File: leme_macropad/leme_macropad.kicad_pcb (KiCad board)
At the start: 4 copper layers, 99.9 x 63.9 mm, 90 parts, among them J1 OLED display, J2 USB_C_Receptacle_USB2.0_16P, SW1 SW_Push, SW2 SW_Push, SW3 SW_Push, SW4 RotaryEncoder_Switch, SW5 SW_Push, SW6 SW_Push, SW7 SW_Push, SW8 SW_Push, SW9 SW_Push, U0 W25Q128JVS, U1 USBLC6-2SC6, U2 NCP1117-3.3_SOT223, U3 RP2040, Y0 ABM8-272-T3

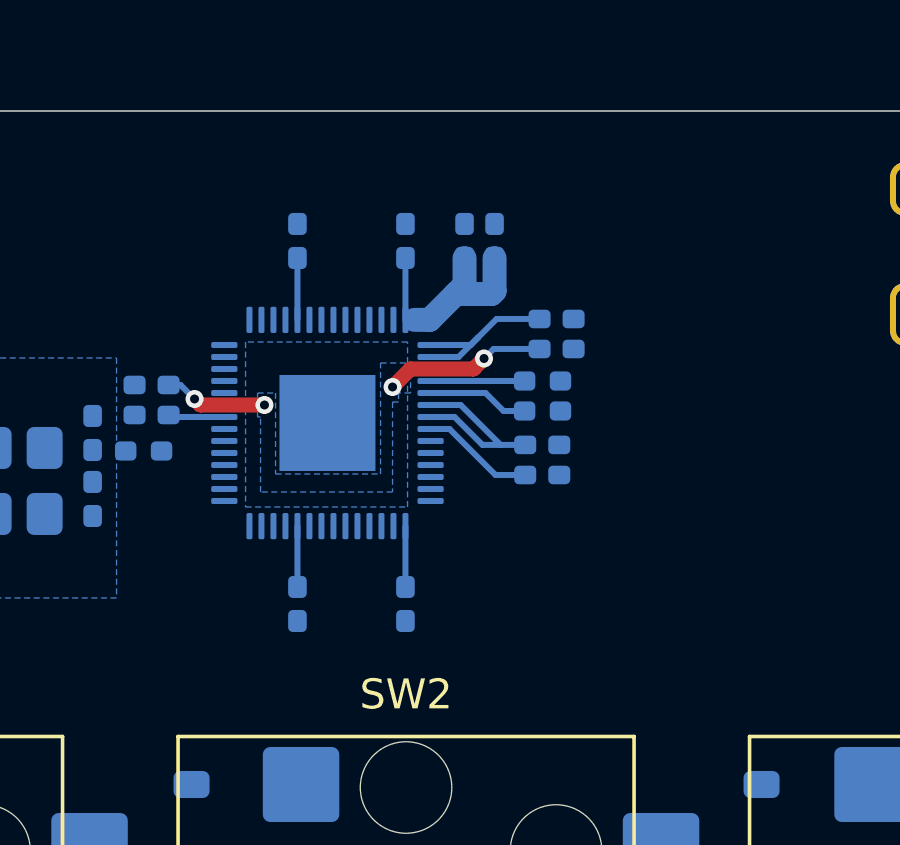
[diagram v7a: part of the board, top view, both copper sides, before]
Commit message: Routes GND for RP2040 and it's decoupling caps
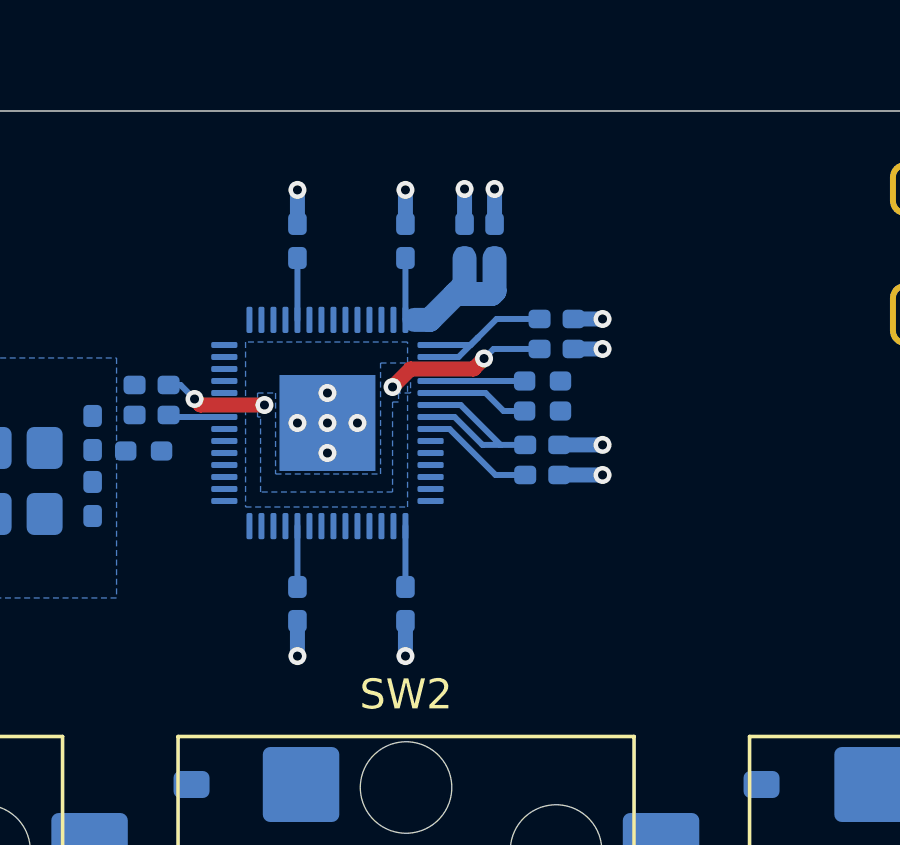
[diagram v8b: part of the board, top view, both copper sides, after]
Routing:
- net GND: track 0.03 -> 12.8 mm, vias 0 -> 15
- added copper zone on In1.Cu, net GND
- added copper zone on In2.Cu, net GND
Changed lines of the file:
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@@
 		)
+	)
+	(via
+		(at 134.43 75.4)
+		(size 0.6)
+		(drill 0.3)
+		(layers "F.Cu" "B.Cu")
+		(net 2)
+	)
+	(via
+		(at 144.6 76.129937)
+		(size 0.6)
+		(drill 0.3)
+		(layers "F.Cu" "B.Cu")
+		(net 2)
+	)
+	(via
+		(at 141 67.6)
+		(size 0.6)
+		(drill 0.3)
+		(layers "F.Cu" "B.Cu")
+		(net 2)
+	)
+	(via
+		(at 134.43 67.63)
+		(size 0.6)
+		(drill 0.3)
+		(layers "F.Cu" "B.Cu")
+		(net 2)
+	)
+	(via
+		(at 140 67.6)
+		(size 0.6)
+		(drill 0.3)
+		(layers "F.Cu" "B.Cu")
+		(net 2)
+	)
+	(via
+		(at 135.43 76.4)
+		(size 0.6)
+		(drill 0.3)
+		(layers "F.Cu" "B.Cu")
+		(net 2)
+	)
+	(via
+		(at 138.03 67.63)
+		(size 0.6)
+		(drill 0.3)
+		(layers "F.Cu" "B.Cu")
+		(net 2)
+	)
+	(via
+		(at 136.43 75.4)
+		(size 0.6)
+		(drill 0.3)
+		(layers "F.Cu" "B.Cu")
+		(net 2)
+	)
+	(via
+		(at 138.03 83.17)
+		(size 0.6)
+		(drill 0.3)
+		(layers "F.Cu" "B.Cu")
+		(net 2)
+	)
+	(via
+		(at 134.43 83.17)
+		(size 0.6)
+		(drill 0.3)
+		(layers "F.Cu" "B.Cu")
+		(net 2)
+	)
+	(via
+		(at 135.43 75.4)
+		(size 0.6)
+		(drill 0.3)
+		(layers "F.Cu" "B.Cu")
+		(net 2)
+	)
+	(via
+		(at 135.43 74.4)
+		(size 0.6)
+		(drill 0.3)
+		(layers "F.Cu" "B.Cu")
+		(net 2)
+	)
+	(via
+		(at 144.6 77.1325)
+		(size 0.6)
+		(drill 0.3)
+		(layers "F.Cu" "B.Cu")
+		(net 2)
+	)
+	(via
+		(at 144.6 72.9325)
+		(size 0.6)
+		(drill 0.3)
+		(layers "F.Cu" "B.Cu")
+		(net 2)
+	)
+	(via
+		(at 144.6 71.9325)
+		(size 0.6)
+		(drill 0.3)
+		(layers "F.Cu" "B.Cu")
+		(net 2)
+	)
+	(segment
+		(start 138.03 83.17)
+		(end 138.03 82)
+		(width 0.5)
+		(layer "B.Cu")
+		(net 2)
+	)
+	(segment
+		(start 144.6 72.9325)
+		(end 143.635 72.9325)
+		(width 0.5)
+		(layer "B.Cu")
+		(net 2)
+	)
+	(segment
+		(start 138.03 67.63)
+		(end 138.03 68.765)
+		(width 0.5)
+		(layer "B.Cu")
+		(net 2)
+	)
+	(segment
+		(start 134.43 67.63)
+		(end 134.43 68.765)
+		(width 0.5)
+		(layer "B.Cu")
+		(net 2)
+	)
+	(segment
+		(start 134.43 83.17)
+		(end 134.43 82)
+		(width 0.5)
+		(layer "B.Cu")
+		(net 2)
+	)
+	(segment
+		(start 141 68.765)
+		(end 141 67.6)
+		(width 0.5)
+		(layer "B.Cu")
+		(net 2)
+	)
+	(segment
+		(start 140 68.765)
+		(end 140 67.6)
+		(width 0.5)
+		(layer "B.Cu")
+		(net 2)
+	)
+	(segment
+		(start 135.43 75.4)
+		(end 135.43 74.43)
+		(width 0.5)
+		(layer "B.Cu")
+		(net 2)
 	)
 	(segment
 		(start 135.43 75.4)
 		(end 135.4 75.4)
-		(width 0.8)
+		(width 0.5)
+		(layer "B.Cu")
+		(net 2)
+	)
+	(segment
+		(start 144.6 71.9325)
+		(end 143.635 71.9325)
+		(width 0.5)
+		(layer "B.Cu")
+		(net 2)
+	)
+	(segment
+		(start 135.43 74.43)
+		(end 135.4 74.4)
+		(width 0.5)
+		(layer "B.Cu")
+		(net 2)
+	)
+	(segment
+		(start 144.6 76.129937)
+		(end 143.157144 76.129937)
+		(width 0.5)
+		(layer "B.Cu")
+		(net 2)
+	)
+	(segment
+		(start 144.6 77.1325)
+		(end 143.157144 77.1325)
+		(width 0.5)
 		(layer "B.Cu")
 		(net 2)
@@
 		(layer "B.Cu")
 		(hatch edge 0.5)
-		(priority 4)
+		(priority 5)
 		(connect_pads
 			(clearance 0.5)
@@
 			(thermal_gap 0.5)
 			(thermal_bridge_width 0.5)
+			(smoothing fillet)
+			(radius 0.5)
 		)
 		(polygon
@@
 			)
 		)
+	)
+	(zone
+		(net 2)
+		(net_name "GND")
+		(layers "In1.Cu" "In2.Cu")
+		(hatch edge 0.5)
+		(connect_pads
+			(clearance 0.15)
+		)
+		(min_thickness 0.25)
+		(filled_areas_thickness no)
+		(fill yes
+			(thermal_gap 0.5)
+			(thermal_bridge_width 0.5)
+		)
+		(polygon
+			(pts
+				(xy 109 65) (xy 109 122) (xy 175 122) (xy 179 126) (xy 186 129) (xy 195 129) (xy 201 126) (xy 206 121)
+				(xy 208 117) (xy 209 113) (xy 209 107) (xy 207 101) (xy 204 97) (xy 202 95) (xy 196 91) (xy 195 90)
+				(xy 195 65)
+			)
+		)
